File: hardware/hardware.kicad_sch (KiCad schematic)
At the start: 2 parts, among them J1 Conn_02x03_Odd_Even, U1 CH32V003FxPx

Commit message: feat: add routes
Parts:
- added C1: 10uF, Capacitor_SMD:C_0603_1608Metric, symbol Device:C
- added D1, D2, D3: LED, footprints:LYT77K-K2M1, symbol Device:LED
- added D10, D11, D4, D5, D6, D7, D8, D9: LED, LED_SMD:LED_0402_1005Metric, symbol Device:LED
- added R1, R10, R11, R2, R3, R4, R5, R6, R7, R8, R9: 330, Resistor_SMD:R_0402_1005Metric_Pad0.72x0.64mm_HandSolder, symbol Device:R
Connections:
- net +3.3V: now also C1.1
- net GND: now also C1.2, D10.1 (K), D11.1 (K), D2.1 (K), D4.1 (K), D5.1 (K), D6.1 (K), D7.1 (K), D8.1 (K), D9.1 (K), R1.1, R3.1
- net LED_4: now reaches U1.1 (PD4)
- net LED_4: now also R7.2
- net LED_7: now reaches U1.10 (PC0)
- net LED_7: now also R10.2
- net LED_5: now reaches U1.11 (PC1)
- net LED_5: now also R8.2
- net LED_8: now reaches U1.12 (PC2)
- net LED_8: now also R11.2
- net LED_1: now reaches U1.2 (PD5)
- net LED_1: now also R4.2
- net LED_3: now reaches U1.20 (PD3)
- net LED_3: now also R6.2
- net LED_2: now reaches U1.3 (PD6)
- net LED_2: now also R5.2
- net LED_6: now reaches U1.4 (PD7)
- net LED_6: now also R9.2
- net RIGHT_EYE: now reaches U1.5 (PA1)
- net RIGHT_EYE: now also D1.2 (A)
- net NOSE: now reaches U1.6 (PA2)
- net NOSE: now also D3.2 (A)
- net LEFT_EYE: now reaches U1.8 (PD0)
- net LEFT_EYE: now also R2.2
- new net: D10.2 (A), R10.1
- new net: D5.2 (A), R5.1
- new net: D4.2 (A), R4.1
- new net: D8.2 (A), R8.1
- new net: D6.2 (A), R6.1
- new net: D1.1 (K), R1.2
- new net: D2.2 (A), R2.1
- new net: D9.2 (A), R9.1
- new net: D3.1 (K), R3.2
- new net: D11.2 (A), R11.1
- new net: D7.2 (A), R7.1
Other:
- note added: "LEDS"
- moved on the sheet: J1

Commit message: feat: add vias
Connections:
- no-connect marks 3 -> 9
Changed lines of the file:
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@@
+	)
+	(no_connect
+		(at 76.2 50.8)
+	)
+	(no_connect
+		(at 96.52 40.64)
 	)
 	(no_connect
 		(at 170.18 41.91)
+	)
+	(no_connect
+		(at 76.2 43.18)
+	)
+	(no_connect
+		(at 76.2 53.34)
+	)
+	(no_connect
+		(at 76.2 48.26)
 	)
 	(no_connect
@@
 		(at 157.48 41.91)
 	)
+	(no_connect
+		(at 76.2 45.72)
+	)
 	(wire

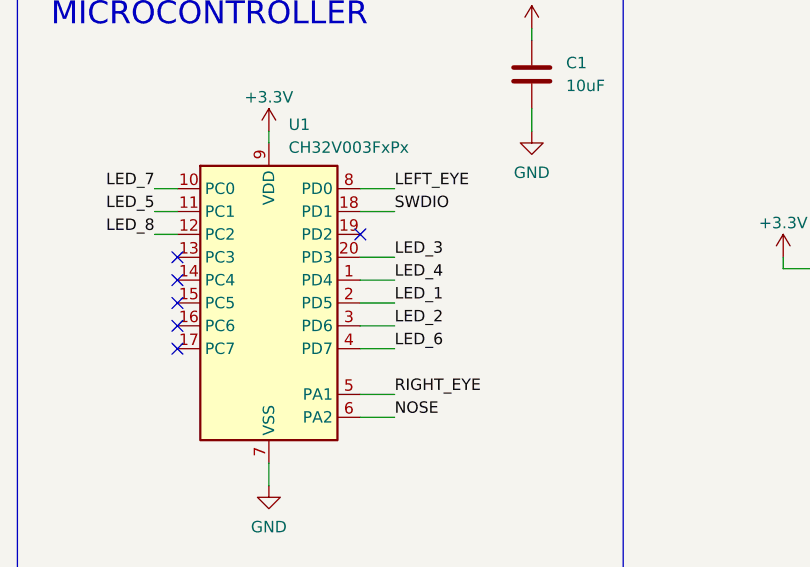
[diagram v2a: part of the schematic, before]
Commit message: refactor(hw): remove routes
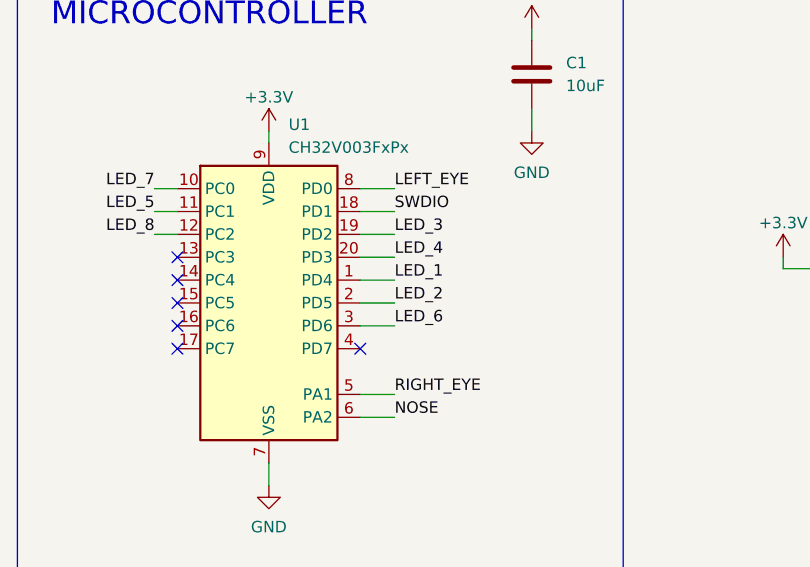
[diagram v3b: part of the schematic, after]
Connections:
- net LED_1: now also U1.1 (PD4); no longer U1.2 (PD5)
- net LED_2: now also U1.2 (PD5); no longer U1.3 (PD6)
- net LED_3: now also U1.19 (PD2); no longer U1.20 (PD3)
- net LED_4: now also U1.20 (PD3); no longer U1.1 (PD4)
- net LED_6: now also U1.3 (PD6); no longer U1.4 (PD7)

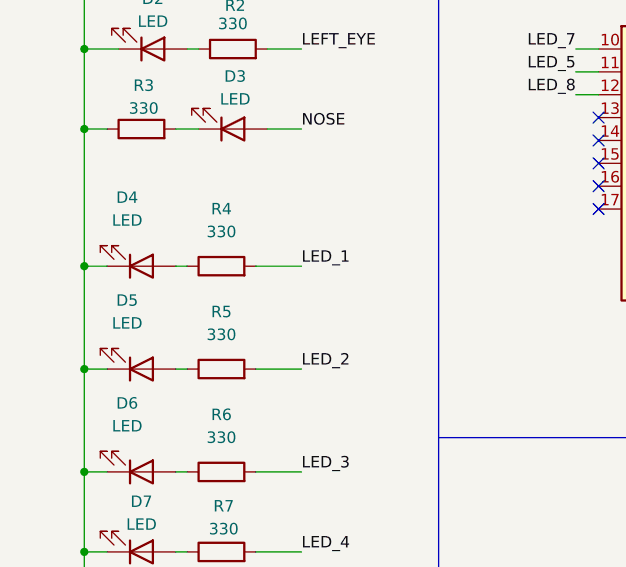
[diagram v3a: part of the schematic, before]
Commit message: feat(hw): add qr and components number
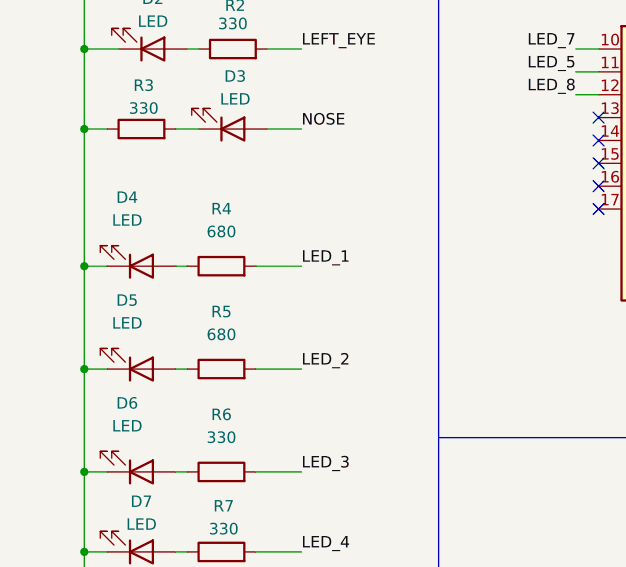
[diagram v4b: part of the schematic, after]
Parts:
- C1: LCSC# (none) -> C5137483
- D10, D11, D6, D7, D8, D9: LCSC# (none) -> C779449
- D4, D5: LCSC# (none) -> C20613596
- R1, R10, R11, R2, R3, R6, R7, R8, R9: LCSC# (none) -> C49653054
- R4, R5: value 330 -> 680; LCSC# (none) -> C137948
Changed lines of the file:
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@@
+			)
+		)
+		(property "LCSC#" "C49653054"
+			(at 34.29 119.38 90)
+			(effects
+				(font
+					(size 1.27 1.27)
+				)
+				(hide yes)
 			)
 		)
@@
 			)
 		)
-		(property "Value" "330"
+		(property "Value" "680"
 			(at 34.29 67.31 90)
 			(effects
@@
 		(property "Description" "Resistor"
 			(at 34.29 71.12 0)
+			(effects
+				(font
+					(size 1.27 1.27)
+				)
+				(hide yes)
+			)
+		)
+		(property "LCSC#" "C137948"
+			(at 34.29 71.12 90)
 			(effects
 				(font
@@
 			)
 		)
-		(property "Value" "330"
+		(property "Value" "680"
 			(at 34.29 55.88 90)
 			(effects
@@
 			)
 		)
+		(property "LCSC#" "C137948"
+			(at 34.29 59.69 90)
+			(effects
+				(font
+					(size 1.27 1.27)
+				)
+				(hide yes)
+			)
+		)
 		(pin "2"
 		)
@@
 		(property "Description" "Resistor"
 			(at 34.29 100.33 0)
+			(effects
+				(font
+					(size 1.27 1.27)
+				)
+				(hide yes)
+			)
+		)
+		(property "LCSC#" "C49653054"
+			(at 34.29 100.33 90)
 			(effects
 				(font
@@
 			)
 		)
+		(property "LCSC#" "C779449"
+			(at 25.4 82.55 0)
+			(effects
+				(font
+					(size 1.27 1.27)
+				)
+				(hide yes)
+			)
+		)
 		(pin "1"
 		)
@@
 			)
 		)
+		(property "LCSC#" "C49653054"
+			(at 25.4 26.67 90)
+			(effects
+				(font
+					(size 1.27 1.27)
+				)
+				(hide yes)
+			)
+		)
 		(pin "2"
 		)
@@
 		(property "Description" "Resistor"
 			(at 35.56 35.56 0)
+			(effects
+				(font
+					(size 1.27 1.27)
+				)
+				(hide yes)
+			)
+		)
+		(property "LCSC#" "C49653054"
+			(at 35.56 35.56 90)
 			(effects
 				(font
@@
 			)
 		)
+		(property "LCSC#" "C779449"
+			(at 25.4 109.22 0)
+			(effects
+				(font
+					(size 1.27 1.27)
+				)
+				(hide yes)
+			)
+		)
 		(pin "1"
 		)
@@
 		(property "Description" "Resistor"
 			(at 25.4 44.45 0)
+			(effects
+				(font
+					(size 1.27 1.27)
+				)
+				(hide yes)
+			)
+		)
+		(property "LCSC#" "C49653054"
+			(at 25.4 44.45 90)
 			(effects
 				(font
@@
 			)
 		)
+		(property "LCSC#" "C20613596"
+			(at 25.4 59.69 0)
+			(effects
+				(font
+					(size 1.27 1.27)
+				)
+				(hide yes)
+			)
+		)
 		(pin "1"
 		)
@@
 			)
 		)
+		(property "LCSC#" "C20613596"
+			(at 25.4 71.12 0)
+			(effects
+				(font
+					(size 1.27 1.27)
+				)
+				(hide yes)
+			)
+		)
 		(pin "1"
 		)
@@
 			)
 		)
+		(property "LCSC#" "C779449"
+			(at 25.4 119.38 0)
+			(effects
+				(font
+					(size 1.27 1.27)
+				)
+				(hide yes)
+			)
+		)
 		(pin "1"
 		)
@@
 			)
 		)
+		(property "LCSC#" "C779449"
+			(at 25.4 128.27 0)
+			(effects
+				(font
+					(size 1.27 1.27)
+				)
+				(hide yes)
+			)
+		)
 		(pin "1"
 		)
@@
 		(property "Description" "Resistor"
 			(at 34.29 91.44 0)
+			(effects
+				(font
+					(size 1.27 1.27)
+				)
+				(hide yes)
+			)
+		)
+		(property "LCSC#" "C49653054"
+			(at 34.29 91.44 90)
 			(effects
 				(font
@@
 			)
 		)
+		(property "LCSC#" "C49653054"
+			(at 34.29 109.22 90)
+			(effects
+				(font
+					(size 1.27 1.27)
+				)
+				(hide yes)
+			)
+		)
 		(pin "2"
 		)
@@
 			)
 		)
+		(property "LCSC#" "C779449"
+			(at 25.4 100.33 0)
+			(effects
+				(font
+					(size 1.27 1.27)
+				)
+				(hide yes)
+			)
+		)
 		(pin "1"
 		)
@@
 			)
 		)
+		(property "LCSC#" "C49653054"
+			(at 34.29 82.55 90)
+			(effects
+				(font
+					(size 1.27 1.27)
+				)
+				(hide yes)
+			)
+		)
 		(pin "2"
 		)
@@
 		(property "Description" "Resistor"
 			(at 34.29 128.27 0)
+			(effects
+				(font
+					(size 1.27 1.27)
+				)
+				(hide yes)
+			)
+		)
+		(property "LCSC#" "C49653054"
+			(at 34.29 128.27 90)
 			(effects
 				(font
@@
 			)
 		)
+		(property "LCSC#" "C5137483"
+			(at 115.57 22.86 0)
+			(effects
+				(font
+					(size 1.27 1.27)
+				)
+				(hide yes)
+			)
+		)
 		(pin "2"
 		)
@@
 			(at 25.4 91.44 0)
 			(effects
+				(font
+					(size 1.27 1.27)
+				)
+				(hide yes)
+			)
+		)
+		(property "LCSC#" "C779449"
+			(at 25.4 91.44 0)
+			(effects
